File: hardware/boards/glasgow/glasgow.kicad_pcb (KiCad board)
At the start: 4 copper layers, 80 x 49 mm, 240 parts, among them J1 USB_B_Micro, J10 Conn_01x03, J2 Conn_02x10_Odd_Even, J3 Conn_02x10_Odd_Even, J4 Conn_01x02, J5 Conn_02x22_Odd_Even, J6 Conn_01x08, J7 Conn_01x08, J8 Conn_01x08, J9 Conn_01x08, U1 CY7C68013A-56LTX, U10 SN74LVC1T45DRL, U11 SN74LVC1T45DRL, U12 ADC081C021CIMM, U13 DAC081C081CIMK, U14 TPS73101DBV, U15 TPD3S014, U16 SN74LVC1T45DRL, U17 SN74LVC1T45DRL, U18 SN74LVC1T45DRL, U19 PCA6408APW, U2 CAT24M01W, U20 DAC081C081CIMK, U21 ADC081C021CIMM, U22 SN74LVC1T45DRL, U23 SN74LVC1T45DRL, U24 SN74LVC1T45DRL, U25 SN74LVC1T45DRL, U26 SN74LVC1T45DRL, U27 SN74LVC1T45DRL, U28 SN74LVC1T45DRL, U29 SN74LVC1T45DRL, U3 CAT24C256W, U30 ICE40HX8K-BG121, U31 TPS73101DBV, U32 SN74LVC1T45DRL, U33 MG2040, U34 ATECC508A, U35 MG2040, U36 TLV73312PQDRVRQ1, U4 SN74LVC1T45DRL, U5 PCA6408APW, U6 SN74LVC1T45DRL, U7 LM3880MF-1AF, U8 TLV75533PDRVR, U9 SN74LVC1T45DRL, Y1 24M

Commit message: Revert "revC1: update PCB from schematic (fix regulator values)"
This reverts commit 70646eb11b521e80def833d12eeeb0baf59ca1c9.
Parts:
- U36: value TLV73312PQDRVRQ1 -> TLV75533PDRVR
- U8: value TLV75533PDRVR -> TLV73312PQDRVRQ1
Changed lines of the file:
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@@
-(kicad_pcb (version 20171130) (host pcbnew 5.1.4)
+(kicad_pcb (version 20171130) (host pcbnew 5.1.0)
   (general
     (thickness 1.6)
@@
       (effects (font (size 0.8 0.8) (thickness 0.15)))
     )
-    (fp_text value TLV73312PQDRVRQ1 (at -5.7 1.8 180) (layer F.Fab)
+    (fp_text value TLV75533PDRVR (at -4.7 1.7 180) (layer F.Fab)
       (effects (font (size 1 1) (thickness 0.15)))
     )
@@
       (effects (font (size 0.8 0.8) (thickness 0.15)))
     )
-    (fp_text value TLV75533PDRVR (at -4.2 1.8 180) (layer F.Fab)
+    (fp_text value TLV73312PQDRVRQ1 (at -6.2 1.7 180) (layer F.Fab)
       (effects (font (size 1 1) (thickness 0.15)))
     )

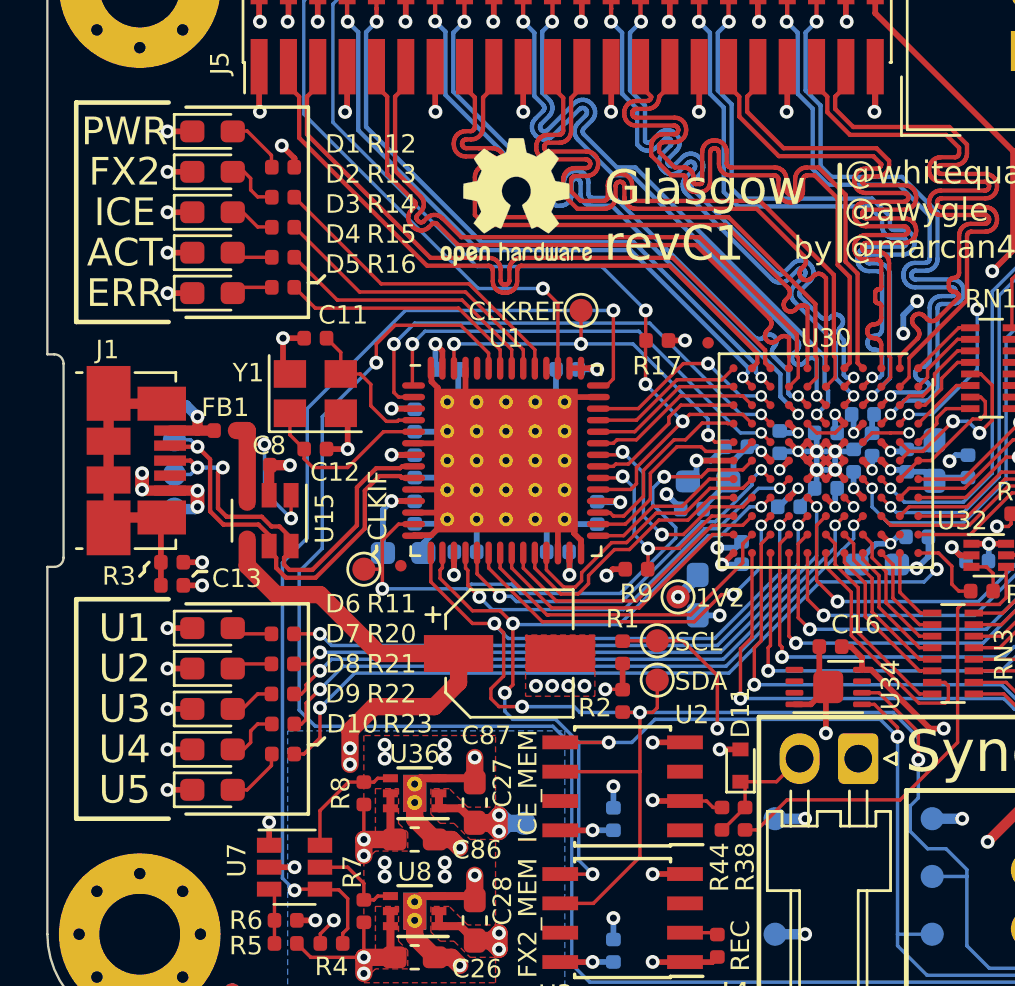
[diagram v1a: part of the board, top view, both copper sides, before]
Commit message: Update the PCB to use USB-C
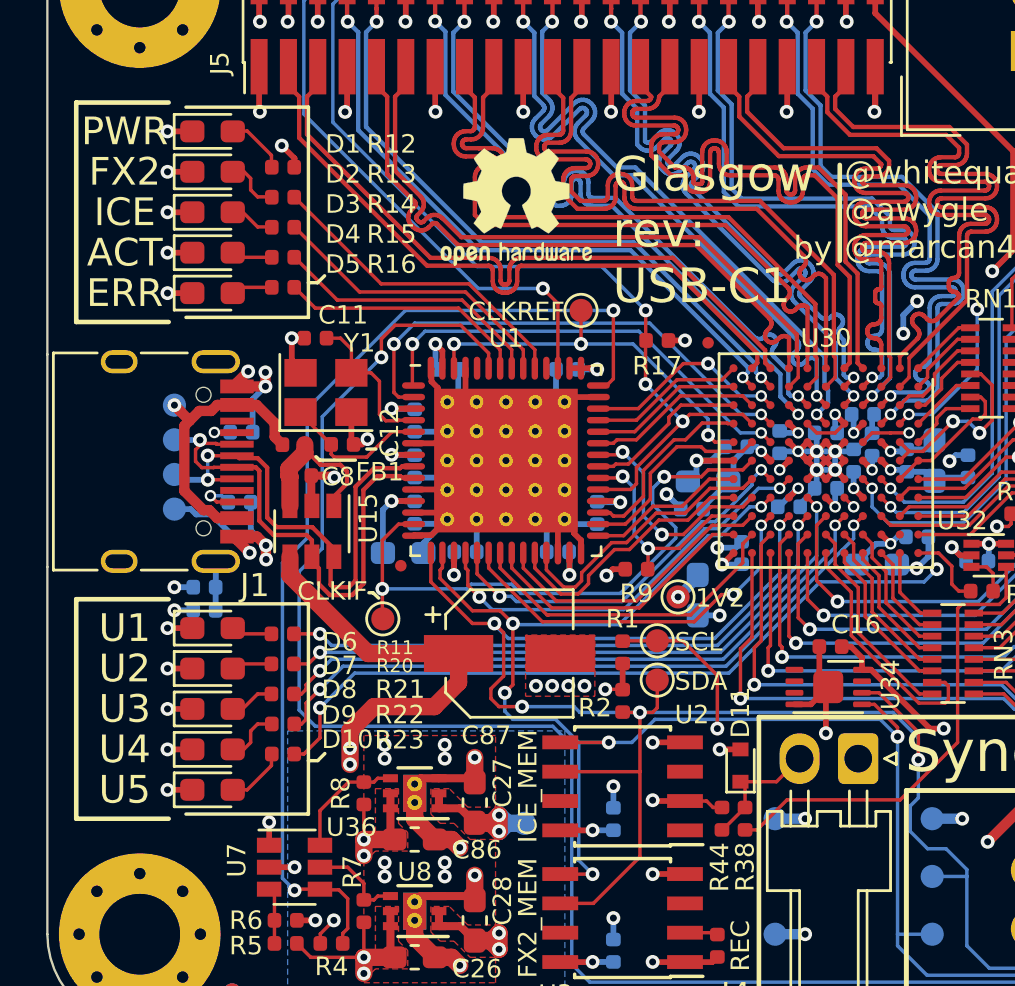
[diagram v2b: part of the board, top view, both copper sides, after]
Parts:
- added R52: 5k1, Resistor_SMD:R_0402_1005Metric, B.Cu at (58.4, 94.3)
- added R53: 5k1, Resistor_SMD:R_0402_1005Metric, B.Cu at (58.3, 97.3)
- C13, R3: moved to B.Cu
- J1: value USB_B_Micro -> USB_C_Receptacle_USB2.0; footprint Connector_USB:USB_Micro-B_Molex_47346-0001 -> Connector_USB_git:USB_C_Receptacle_HRO_TYPE-C-31-M-12
- U36: value TLV75533PDRVR -> TLV73312PQDRVRQ1
- U8: value TLV73312PQDRVRQ1 -> TLV75533PDRVR
- moved FB1 3.02 mm to (60.7, 94.8)
- moved TP7 2.30 mm to (64.5, 102.3)
- moved U15 1.91 mm to (61.5, 98.6)
- moved C8 1.85 mm to (60.9, 96.2)
- moved C13 1.77 mm to (56.8, 102.0), turned to 180 degrees
- moved R3 1.77 mm to (56.8, 101.0), turned to 180 degrees
- moved C12 1.19 mm to (62.8, 94.8)
- moved Y1 0.46 mm to (62.1, 92.5)
- moved J1 0.31 mm to (54.2, 95.5)
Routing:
- net /SHLD: track 15.1 -> 2.12 mm
- net Net-(FB1-Pad1): track 3.71 -> 13.1 mm
- net GND: track 262.0 -> 270.1 mm, vias 116 -> 118
- net /USB_N: track 18.7 -> 22.3 mm
- net /USB_P: track 18.9 -> 22.1 mm
- net /VUSB: track 9.50 -> 6.84 mm, vias 2 -> 0
- net +5V: track 167.8 -> 165.4 mm
- net Net-(J1-PadB5): track 0.00 -> 2.15 mm, vias 0 -> 1
- net Net-(J1-PadA5): track 0.00 -> 1.67 mm, vias 0 -> 1
- net /XTALOUT: track 6.37 -> 7.55 mm
- net /XTALIN: track 7.76 -> 7.00 mm
- net /CLKIF: track 25.8 -> 26.4 mm
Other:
- outline, holes or cut-outs redrawn
- board text added: "Glasgow rev: USB-C1"
- board text removed: "Glasgow revC1"

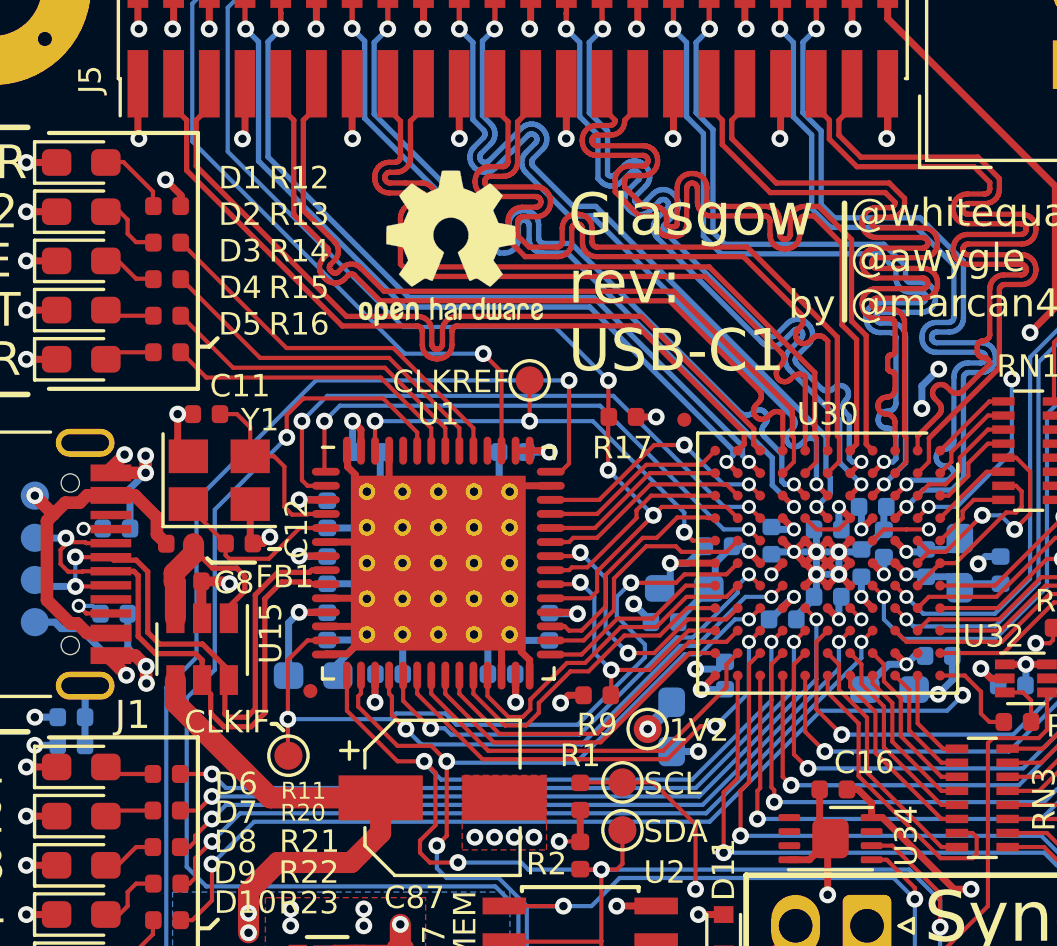
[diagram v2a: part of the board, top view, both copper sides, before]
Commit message: silkscreen fixes and revUSB-C1 production files
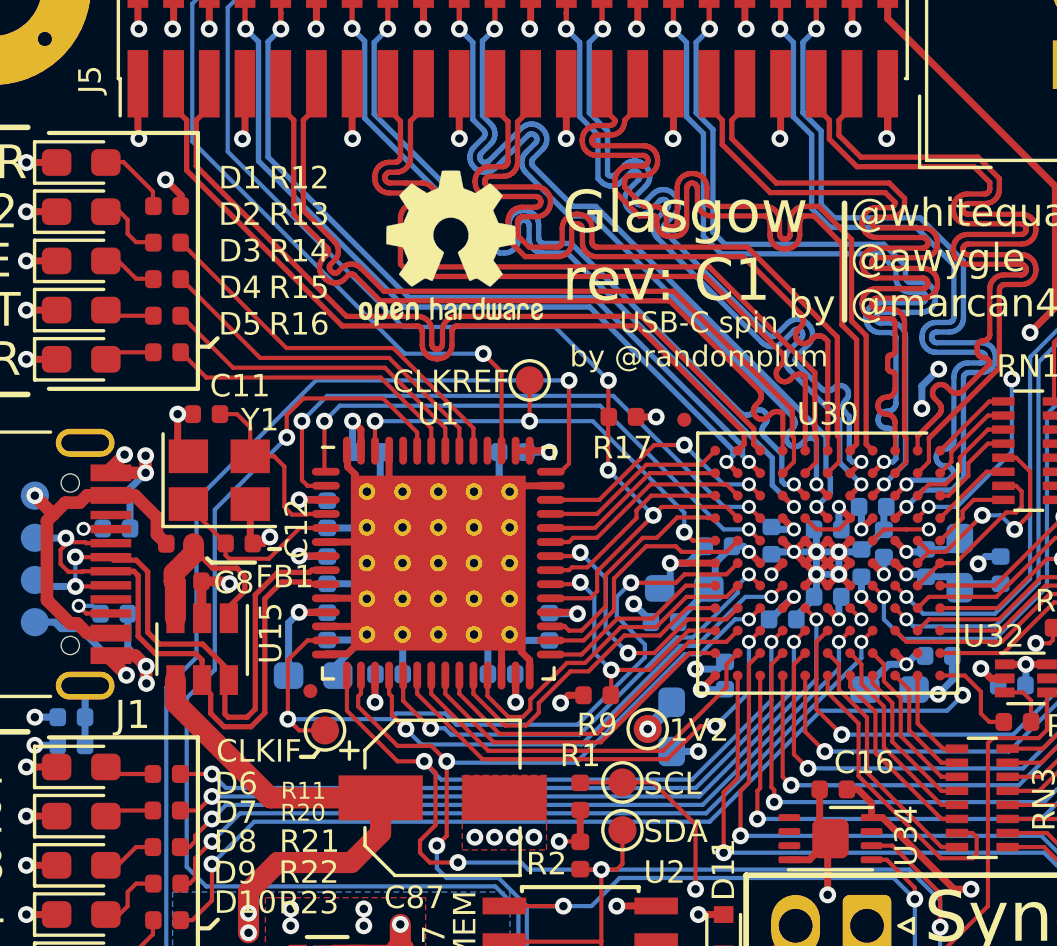
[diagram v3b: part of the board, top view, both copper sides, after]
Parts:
- moved TP7 1.58 mm to (65.8, 101.5)
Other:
- board text added: "Glasgow rev: C1"
- board text added: "USB-C spin by @randomplum"
- board text removed: "Glasgow rev: USB-C1"
